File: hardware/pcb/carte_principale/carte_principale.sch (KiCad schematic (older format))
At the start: 20 parts, among them J1 Arduino_UNO_R3, J2 Conn_01x02, J3 Conn_01x02, P1 TE-FFC-10-0.5, P2 TE-FFC-10-0.5, U1 ESP-WROOM-02, U2 LSM6DS3, U3 BMP280, U4 74AHCT1G04, U5 74AHC1G125, U6 74LS166, U7 LIS2MDL

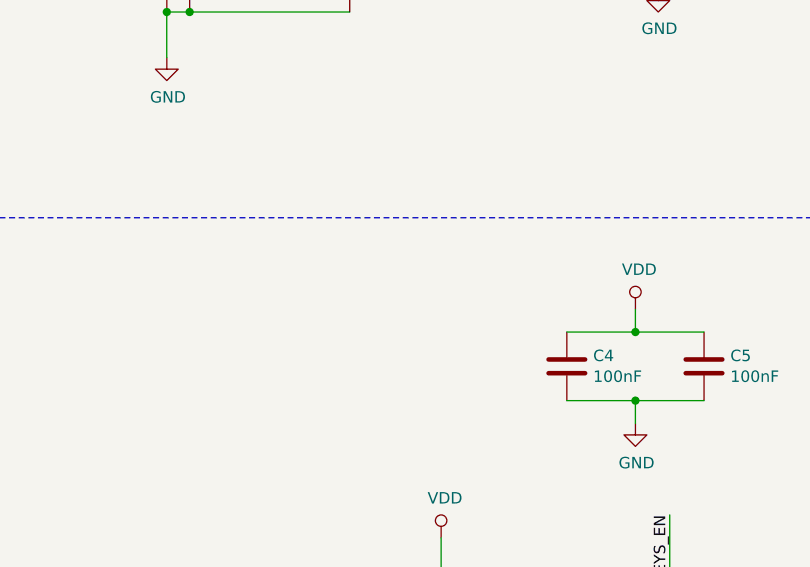
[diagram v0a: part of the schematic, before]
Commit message: ajout des pcb gauche et droit
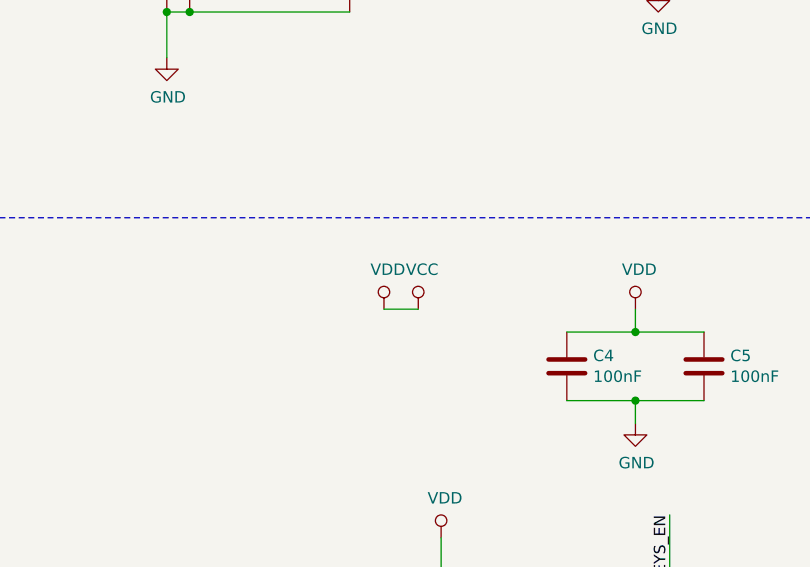
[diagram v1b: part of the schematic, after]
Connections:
- net labels added: VCC
- wire segments 130 -> 131
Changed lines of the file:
@@
 Wire Wire Line
 	6750 4000 7050 4000
+$Comp
+L power:VDD #PWR?
+U 1 1 5C7700B4
+P 5650 3900
+F 0 "#PWR?" H 5650 3750 50  0001 C CNN
+F 1 "VDD" H 5667 4073 50  0000 C CNN
+F 2 "" H 5650 3900 50  0001 C CNN
+F 3 "" H 5650 3900 50  0001 C CNN
+	1    5650 3900
+	1    0    0    -1
+$EndComp
+$Comp
+L power:VCC #PWR?
+U 1 1 5C7754BD
+P 5800 3900
+F 0 "#PWR?" H 5800 3750 50  0001 C CNN
+F 1 "VCC" H 5817 4073 50  0000 C CNN
+F 2 "" H 5800 3900 50  0001 C CNN
+F 3 "" H 5800 3900 50  0001 C CNN
+	1    5800 3900
+	1    0    0    -1
+$EndComp
+Wire Wire Line
+	5650 3900 5800 3900
 $EndSCHEMATC

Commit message: mise a jour des pcb et design mecaniques
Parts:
- added Logo1: LOGO, Insa:insa-image, symbol insa-sym:LOGO
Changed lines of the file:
@@
 encoding utf-8
 Sheet 1 1
-Title ""
-Date ""
-Rev ""
+Title "Carte Principale"
+Date "2019-04-26"
+Rev "02A"
 Comp ""
 Comment1 ""
@@
 	6750 4000 7050 4000
 $Comp
-L power:VDD #PWR?
+L power:VDD #PWR0120
 U 1 1 5C7700B4
 P 5650 3900
-F 0 "#PWR?" H 5650 3750 50  0001 C CNN
+F 0 "#PWR0120" H 5650 3750 50  0001 C CNN
 F 1 "VDD" H 5667 4073 50  0000 C CNN
 F 2 "" H 5650 3900 50  0001 C CNN
@@
 $EndComp
 $Comp
-L power:VCC #PWR?
+L power:VCC #PWR0121
 U 1 1 5C7754BD
 P 5800 3900
-F 0 "#PWR?" H 5800 3750 50  0001 C CNN
+F 0 "#PWR0121" H 5800 3750 50  0001 C CNN
 F 1 "VCC" H 5817 4073 50  0000 C CNN
 F 2 "" H 5800 3900 50  0001 C CNN
@@
 Wire Wire Line
 	5650 3900 5800 3900
+$Comp
+L insa-sym:LOGO Logo1
+U 1 1 5CC35BF7
+P 7600 6850
+F 0 "Logo1" H 7600 6398 60  0001 C CNN
+F 1 "LOGO" H 7600 7302 60  0001 C CNN
+F 2 "Insa:insa-image" H 7600 6850 50  0001 C CNN
+F 3 "" H 7600 6850 50  0001 C CNN
+	1    7600 6850
+	1    0    0    -1
+$EndComp
 $EndSCHEMATC

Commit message: Commit de sauvegarde
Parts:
- removed U4: 74AHCT1G04, Package_TO_SOT_SMD:SOT-353_SC-70-5, symbol 74xGxx:74AHCT1G04
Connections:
- net labels added: BMP280_EN, KEYS_LOAD, KEY_RST, LIS2MDL_IT, LSM6DS3_IT
- net labels removed: EN_BMP280, IT_LIS2MDL, IT_LSM6DS3, Key_RST
- wire segments 131 -> 133
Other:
- moved on the sheet: C4, C5
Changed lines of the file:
@@
-$EndComp
-$Comp
-L 74xGxx:74AHCT1G04 U4
-U 1 1 5C62B0A2
-P 4850 6450
-F 0 "U4" H 4850 6150 50  0000 C CNN
-F 1 "74AHCT1G04" H 4850 6050 50  0000 C CNN
-F 2 "Package_TO_SOT_SMD:SOT-353_SC-70-5" H 4850 6450 50  0001 C CNN
-F 3 "http://www.ti.com/lit/sg/scyt129e/scyt129e.pdf" H 4850 6450 50  0001 C CNN
-	1    4850 6450
-	1    0    0    -1
 $EndComp
 $Comp
@@
 L power:VDD #PWR0105
 U 1 1 5C63EAB9
-P 6950 1400
-F 0 "#PWR0105" H 6950 1250 50  0001 C CNN
-F 1 "VDD" H 6967 1573 50  0000 C CNN
-F 2 "" H 6950 1400 50  0001 C CNN
-F 3 "" H 6950 1400 50  0001 C CNN
-	1    6950 1400
+P 8250 2100
+F 0 "#PWR0105" H 8250 1950 50  0001 C CNN
+F 1 "VDD" H 8267 2273 50  0000 C CNN
+F 2 "" H 8250 2100 50  0001 C CNN
+F 3 "" H 8250 2100 50  0001 C CNN
+	1    8250 2100
 	1    0    0    -1
 $EndComp
@@
 	6400 5450 6600 5450
 Wire Wire Line
-	5100 6450 5400 6450
-Wire Wire Line
 	5400 6650 4550 6650
 Wire Wire Line
@@
 Wire Wire Line
 	4550 6450 4200 6450
-Connection ~ 4550 6450
 Wire Wire Line
 	7150 5450 7750 5450
@@
 Key_B
 Text Label 3400 4700 0    50   ~ 0
-Key_RST
+KEY_RST
 Text Label 3350 4300 0    50   ~ 0
 Audio_Right_1
@@
 Audio_Right_2
 Wire Wire Line
-	3950 4400 3950 4600
-Wire Wire Line
 	3950 5200 3400 5200
 Wire Wire Line
@@
 Connection ~ 3400 5200
 Wire Wire Line
-	3300 4600 3950 4600
-Connection ~ 3950 4600
-Wire Wire Line
-	3950 4600 3950 5200
-Wire Wire Line
-	3950 6150 3950 6350
-Wire Wire Line
 	3950 6950 3450 6950
 Wire Wire Line
@@
 Wire Wire Line
 	3950 6450 3950 6950
-Wire Wire Line
-	3300 6350 3950 6350
-Connection ~ 3950 6350
-Wire Wire Line
-	3950 6350 3950 6450
 Wire Wire Line
 	5400 5550 4750 5550
@@
 Text Label 8400 2200 0    50   ~ 0
 KEYS_EN
-Wire Wire Line
-	5100 6550 5400 6550
-Text Label 5100 6550 0    50   ~ 0
+Text Label 4800 6550 0    50   ~ 0
 SPI_SCK
 Wire Wire Line
@@
 SPI_MISO
 Text Label 5950 2100 0    50   ~ 0
-EN_BMP280
+BMP280_EN
 Wire Wire Line
 	4100 2300 4000 2300
@@
 	5300 1700 5700 1700
 Text Label 5350 1700 0    50   ~ 0
-IT_LSM6DS3
+LSM6DS3_IT
 Wire Wire Line
 	1600 1900 1000 1900
@@
 I2C_SDA
 Text Label 1050 2250 0    50   ~ 0
-IT_LIS2MDL
+LIS2MDL_IT
 Wire Wire Line
 	1600 2100 1500 2100
@@
 	8900 2800 8350 2800
 Text Label 8400 2800 0    50   ~ 0
-EN_BMP280
+BMP280_EN
 Text Label 8400 2300 0    50   ~ 0
-IT_LSM6DS3
+LSM6DS3_IT
 Text Label 8400 2400 0    50   ~ 0
-IT_LIS2MDL
+LIS2MDL_IT
 Wire Wire Line
 	8900 2900 8350 2900
@@
 L Device:C C5
 U 1 1 5C72BC25
-P 7050 4150
-F 0 "C5" H 7165 4196 50  0000 L CNN
-F 1 "100nF" H 7165 4105 50  0000 L CNN
-F 2 "Capacitor_SMD:C_1206_3216Metric" H 7088 4000 50  0001 C CNN
-F 3 "~" H 7050 4150 50  0001 C CNN
-	1    7050 4150
-	1    0    0    -1
-$EndComp
-$Comp
-L Device:C C4
-U 1 1 5C730929
-P 6450 4150
-F 0 "C4" H 6565 4196 50  0000 L CNN
-F 1 "100nF" H 6565 4105 50  0000 L CNN
-F 2 "Capacitor_SMD:C_1206_3216Metric" H 6488 4000 50  0001 C CNN
-F 3 "~" H 6450 4150 50  0001 C CNN
-	1    6450 4150
+P 6750 4150
+F 0 "C5" H 6865 4196 50  0000 L CNN
+F 1 "100nF" H 6865 4105 50  0000 L CNN
+F 2 "Capacitor_SMD:C_1206_3216Metric" H 6788 4000 50  0001 C CNN
+F 3 "~" H 6750 4150 50  0001 C CNN
+	1    6750 4150
 	1    0    0    -1
 $EndComp
@@
 $EndComp
 Wire Wire Line
-	6450 4000 6750 4000
-Wire Wire Line
-	6450 4300 6750 4300
-Wire Wire Line
 	6750 4300 6750 4400
-Connection ~ 6750 4300
-Wire Wire Line
-	6750 4300 7050 4300
 Wire Wire Line
 	6750 3900 6750 4000
-Connection ~ 6750 4000
-Wire Wire Line
-	6750 4000 7050 4000
 $Comp
 L power:VDD #PWR0120
@@
 	1    0    0    -1
 $EndComp
+Wire Wire Line
+	9900 1800 10450 1800
+Text Label 10050 1800 0    50   ~ 0
+KEY_RST
+Wire Wire Line
+	3950 4400 3950 5200
+Wire Wire Line
+	3950 6150 3950 6450
+Wire Wire Line
+	3300 6350 4050 6350
+Wire Wire Line
+	4050 6350 4050 5900
+Wire Wire Line
+	3300 4600 4050 4600
+Wire Wire Line
+	4050 4600 4050 4200
+$Comp
+L power:VDD #PWR0122
+U 1 1 5CDDD93F
+P 4050 4200
+F 0 "#PWR0122" H 4050 4050 50  0001 C CNN
+F 1 "VDD" H 4067 4373 50  0000 C CNN
+F 2 "" H 4050 4200 50  0001 C CNN
+F 3 "" H 4050 4200 50  0001 C CNN
+	1    4050 4200
+	1    0    0    -1
+$EndComp
+$Comp
+L power:VDD #PWR0123
+U 1 1 5CDE310B
+P 4050 5900
+F 0 "#PWR0123" H 4050 5750 50  0001 C CNN
+F 1 "VDD" H 4067 6073 50  0000 C CNN
+F 2 "" H 4050 5900 50  0001 C CNN
+F 3 "" H 4050 5900 50  0001 C CNN
+	1    4050 5900
+	1    0    0    -1
+$EndComp
+$Comp
+L Device:C C4
+U 1 1 5C730929
+P 7800 1950
+F 0 "C4" H 7915 1996 50  0000 L CNN
+F 1 "100nF" H 7915 1905 50  0000 L CNN
+F 2 "Capacitor_SMD:C_1206_3216Metric" H 7838 1800 50  0001 C CNN
+F 3 "~" H 7800 1950 50  0001 C CNN
+	1    7800 1950
+	1    0    0    -1
+$EndComp
+Wire Wire Line
+	7550 1600 7800 1600
+Wire Wire Line
+	7800 1600 7800 1800
+Connection ~ 7550 1600
+Wire Wire Line
+	7800 2100 7800 2300
+Wire Wire Line
+	7800 2300 7550 2300
+Connection ~ 7550 2300
+Wire Wire Line
+	4750 6450 5400 6450
+Text Label 4800 6450 0    50   ~ 0
+KEYS_LOAD
+Wire Wire Line
+	4750 6550 5400 6550
+Wire Wire Line
+	8900 2700 8350 2700
+Text Label 8400 2700 0    50   ~ 0
+KEYS_LOAD
+$Comp
+L power:VDD #PWR?
+U 1 1 5CE25200
+P 6950 1400
+F 0 "#PWR?" H 6950 1250 50  0001 C CNN
+F 1 "VDD" H 6967 1573 50  0000 C CNN
+F 2 "" H 6950 1400 50  0001 C CNN
+F 3 "" H 6950 1400 50  0001 C CNN
+	1    6950 1400
+	1    0    0    -1
+$EndComp

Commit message: sauvegarde intermediaire
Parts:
- added R1, R2: 10K, Resistor_SMD:R_1206_3216Metric, symbol Device:R
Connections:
- wire segments 133 -> 143
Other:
- note added: "WIFI_RST is open drain, actif low"
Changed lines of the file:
@@
 Title "Carte Principale"
 Date "2019-04-26"
-Rev "02A"
+Rev "02B"
 Comp ""
 Comment1 ""
@@
 D14/D15 = I2C1
 Wire Wire Line
-	9900 3100 10400 3100
-Wire Wire Line
-	9900 3200 10400 3200
-Wire Wire Line
 	8900 1800 8350 1800
 Wire Wire Line
@@
 	4000 1400 4700 1400
 Wire Wire Line
-	4000 1400 4000 2300
+	4000 1400 4000 1700
 Connection ~ 4700 1400
 Wire Wire Line
@@
 	10100 6050 10950 6050
 Wire Wire Line
-	10950 6050 10950 5600
+	10950 6050 10950 5700
 Connection ~ 10100 6050
 Wire Wire Line
 	10100 6050 10100 6000
 Wire Wire Line
-	10950 5300 10950 4800
+	10950 5300 10950 5000
 Wire Wire Line
 	10950 4800 10100 4800
@@
 KEYS_LOAD
 $Comp
-L power:VDD #PWR?
+L power:VDD #PWR0124
 U 1 1 5CE25200
 P 6950 1400
-F 0 "#PWR?" H 6950 1250 50  0001 C CNN
+F 0 "#PWR0124" H 6950 1250 50  0001 C CNN
 F 1 "VDD" H 6967 1573 50  0000 C CNN
 F 2 "" H 6950 1400 50  0001 C CNN
@@
 	1    0    0    -1
 $EndComp
+Wire Wire Line
+	4100 1700 4000 1700
+Connection ~ 4000 1700
+Wire Wire Line
+	4000 1700 4000 2300
+$Comp
+L Device:R R1
+U 1 1 5CE68C07
+P 10500 2950
+F 0 "R1" H 10570 2996 50  0000 L CNN
+F 1 "10K" H 10570 2905 50  0000 L CNN
+F 2 "Resistor_SMD:R_1206_3216Metric" V 10430 2950 50  0001 C CNN
+F 3 "~" H 10500 2950 50  0001 C CNN
+	1    10500 2950
+	1    0    0    -1
+$EndComp
+$Comp
+L Device:R R2
+U 1 1 5CE68CA1
+P 10800 2950
+F 0 "R2" H 10870 2996 50  0000 L CNN
+F 1 "10K" H 10870 2905 50  0000 L CNN
+F 2 "Resistor_SMD:R_1206_3216Metric" V 10730 2950 50  0001 C CNN
+F 3 "~" H 10800 2950 50  0001 C CNN
+	1    10800 2950
+	1    0    0    -1
+$EndComp
+Wire Wire Line
+	10500 2800 10650 2800
+Wire Wire Line
+	10650 2800 10650 2700
+Connection ~ 10650 2800
+Wire Wire Line
+	10650 2800 10800 2800
+Wire Wire Line
+	9900 3100 10500 3100
+Wire Wire Line
+	10800 3200 10800 3100
+Wire Wire Line
+	9900 3200 10800 3200
+$Comp
+L power:VDD #PWR0125
+U 1 1 5CE85BB2
+P 10650 2700
+F 0 "#PWR0125" H 10650 2550 50  0001 C CNN
+F 1 "VDD" H 10667 2873 50  0000 C CNN
+F 2 "" H 10650 2700 50  0001 C CNN
+F 3 "" H 10650 2700 50  0001 C CNN
+	1    10650 2700
+	1    0    0    -1
+$EndComp
+Wire Wire Line
+	10600 5000 10950 5000
+Connection ~ 10950 5000
+Wire Wire Line
+	10950 5000 10950 4800
+Wire Wire Line
+	10600 5700 10950 5700
+Connection ~ 10950 5700
+Wire Wire Line
+	10950 5700 10950 5600
+Text Notes 8600 6150 0    50   ~ 0
+WIFI_RST is open drain, actif low
 $EndSCHEMATC
